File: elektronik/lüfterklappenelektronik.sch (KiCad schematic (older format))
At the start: 96 parts, among them J101 Conn_01x05_Male, J102 Ckmtw_2510S-2P, J103 Conn_LAN_ENC28J60, J104 USB_B_Micro, J105 #Stecker, J106 Ckmtw_2510S-2P, J107 Ckmtw_2510S-2P, J108 Ckmtw_2510S-2P, P101 PWR_BUS_CONN1, P102 #FAN_230VAC_Phase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

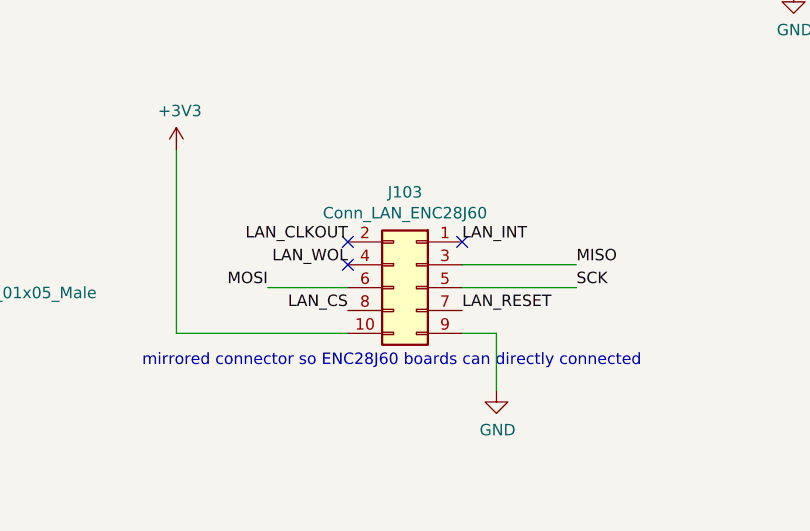
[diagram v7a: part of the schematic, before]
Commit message: fix LAN port
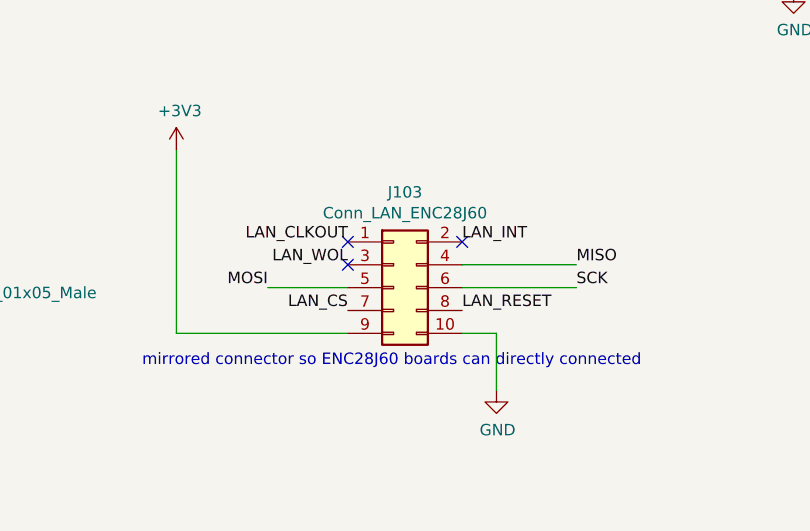
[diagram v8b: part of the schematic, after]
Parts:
- P101, P109: footprint TerminalBlock_RND:TerminalBlock_RND_205-00289_1x04_P5.08mm_Horizontal -> FootprintsTittelbach:WJ2EDGRC-5.08-4P
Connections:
- net +3V3: now also J103.9 (Pin_9); no longer J103.10 (Pin_10)
- net GND: now also J103.10 (Pin_10); no longer J103.9 (Pin_9)
- net LAN_CLKOUT: now also J103.1 (Pin_1); no longer J103.2 (Pin_2)
- net LAN_CS: now also J103.7 (Pin_7); no longer J103.8 (Pin_8)
- net LAN_INT: now also J103.2 (Pin_2); no longer J103.1 (Pin_1)
- net LAN_RESET: now also J103.8 (Pin_8); no longer J103.7 (Pin_7)
- net LAN_WOL: now also J103.3 (Pin_3); no longer J103.4 (Pin_4)
- net MISO: now also J103.4 (Pin_4); no longer J103.3 (Pin_3)
- net MOSI: now also J103.5 (Pin_5); no longer J103.6 (Pin_6)
- net SCK: now also J103.6 (Pin_6); no longer J103.5 (Pin_5)
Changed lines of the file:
@@
 F 0 "P101" H 9650 3250 50  0000 C CNN
 F 1 "PWR_BUS_CONN1" H 9800 3350 50  0000 C CNN
-F 2 "TerminalBlock_RND:TerminalBlock_RND_205-00289_1x04_P5.08mm_Horizontal" H 9450 3300 50  0001 C CNN
+F 2 "FootprintsTittelbach:WJ2EDGRC-5.08-4P" H 9450 3300 50  0001 C CNN
 F 3 "https://datasheet.lcsc.com/szlcsc/1912251635_Ningbo-Kangnex-Elec-WJ2EDGRC-5-08-4P_C8446.pdf" H 9450 3300 50  0001 C CNN
 F 4 "Ningbo Kangnex Elec" H 9450 3300 50  0001 C CNN "MF"
@@
 Text Notes 12450 1150 0    50   ~ 0
 Power Use:\n0120mA ... Gabellichtschranken\n1000mA ... ESP32\n0010mA  ... Green LED\n0011mA  ... IR Led inside FAN SSR
-$Comp
-L Connector_Generic:Conn_02x05_Odd_Even J103
-U 1 1 60133D2E
-P 4750 10400
-F 0 "J103" H 4800 10817 50  0000 C CNN
-F 1 "Conn_LAN_ENC28J60" H 4800 10726 50  0000 C CNN
-F 2 "Connector_PinSocket_2.54mm:PinSocket_2x05_P2.54mm_Vertical_SMD" H 4750 10400 50  0001 C CNN
-F 3 "~" H 4750 10400 50  0001 C CNN
-	1    4750 10400
-	-1   0    0    -1
-$EndComp
 Text Label 4450 10200 2    50   ~ 0
 LAN_CLKOUT
@@
 $EndComp
 Wire Wire Line
-	4950 10600 5100 10600
-Wire Wire Line
 	5100 10600 5100 10850
 $Comp
@@
 MOSI
 Wire Wire Line
-	4950 10300 5450 10300
-Wire Wire Line
 	4100 10400 4450 10400
 Text Label 5450 10400 0    50   ~ 0
 SCK
-Wire Wire Line
-	5450 10400 4950 10400
 NoConn ~ 4450 10200
 NoConn ~ 4950 10200
@@
 F 0 "P109" H 10569 2925 50  0000 C CNN
 F 1 "PWR_BUS_CONN2" H 10569 3016 50  0000 C CNN
-F 2 "TerminalBlock_RND:TerminalBlock_RND_205-00289_1x04_P5.08mm_Horizontal" H 10650 3300 50  0001 C CNN
+F 2 "FootprintsTittelbach:WJ2EDGRC-5.08-4P" H 10650 3300 50  0001 C CNN
 F 3 "https://datasheet.lcsc.com/szlcsc/1912251635_Ningbo-Kangnex-Elec-WJ2EDGRC-5-08-4P_C8446.pdf" H 10650 3300 50  0001 C CNN
 F 4 "Ningbo Kangnex Elec" H 10650 3300 50  0001 C CNN "MF"
@@
 	1    0    0    -1
 $EndComp
+Wire Wire Line
+	5450 10400 4950 10400
+Wire Wire Line
+	4950 10300 5450 10300
+Wire Wire Line
+	4950 10600 5100 10600
+$Comp
+L Connector_Generic:Conn_02x05_Odd_Even J103
+U 1 1 60133D2E
+P 4650 10400
+F 0 "J103" H 4700 10817 50  0000 C CNN
+F 1 "Conn_LAN_ENC28J60" H 4700 10726 50  0000 C CNN
+F 2 "Connector_PinSocket_2.54mm:PinSocket_2x05_P2.54mm_Vertical_SMD" H 4650 10400 50  0001 C CNN
+F 3 "~" H 4650 10400 50  0001 C CNN
+	1    4650 10400
+	1    0    0    -1
+$EndComp
